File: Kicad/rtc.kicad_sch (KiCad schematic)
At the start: 6 parts, among them U1101 MCP7940N, Y1101 32,768 Hz

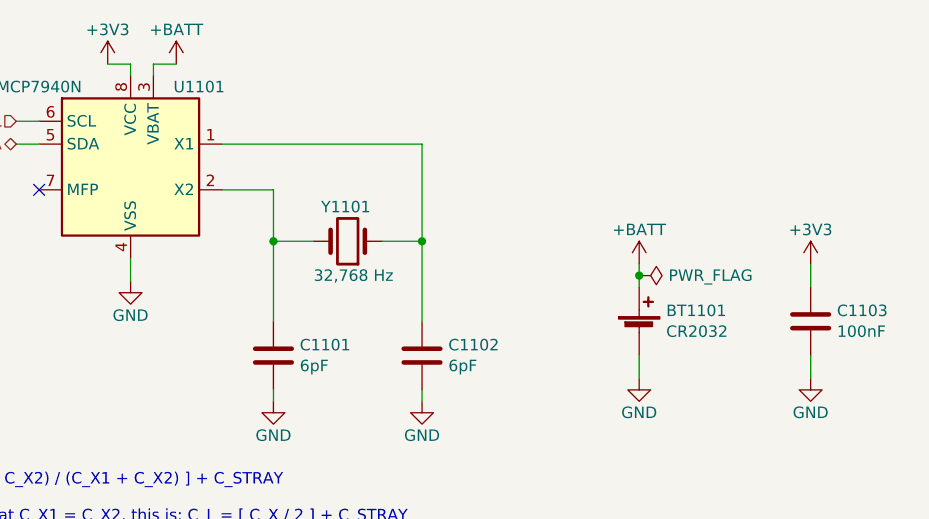
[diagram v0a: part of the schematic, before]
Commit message: Update schematic files to Kicad 6.
Had to fix some symbols which didn't have perfect matches in K6.
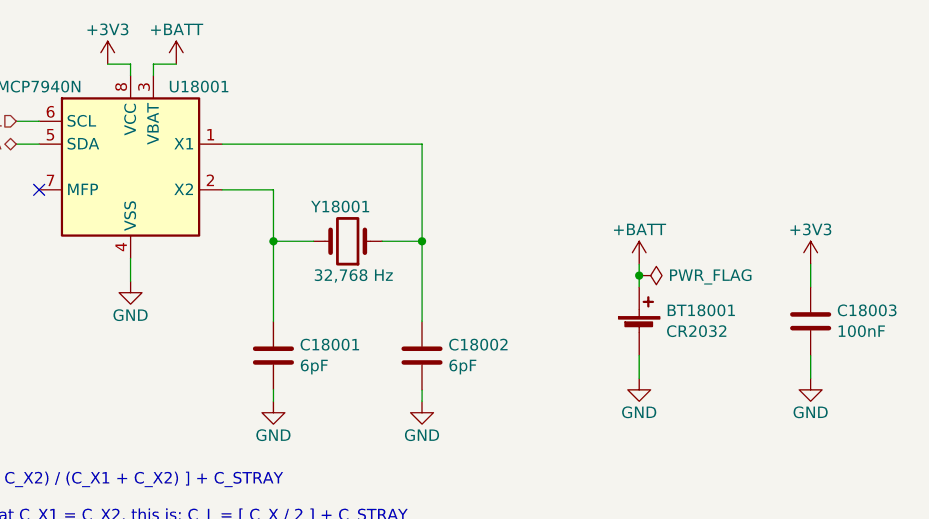
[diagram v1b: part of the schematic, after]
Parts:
- U18001: renamed from U1101; symbol Neotron-Common-Hardware-rescue:MCP7940N-xP-Timer -> Timer_RTC:MCP7940N-xP
- renumbered BT1101 to BT18001, C1101 to C18001, C1102 to C18002, C1103 to C18003, Y1101 to Y18001
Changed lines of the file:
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@@
   (symbol (lib_id "power:+3V3") (at 179.07 78.74 0) (unit 1)
     (in_bom yes) (on_board yes)
-    (property "Reference" "#PWR01108" (id 0) (at 179.07 82.55 0)
+    (property "Reference" "#PWR018008" (id 0) (at 179.07 82.55 0)
       (effects (font (size 1.27 1.27)) hide)
     )
@@
   (symbol (lib_id "Device:C") (at 179.07 85.09 0) (unit 1)
     (in_bom yes) (on_board yes)
-    (property "Reference" "C1103" (id 0) (at 181.991 83.9216 0)
+    (property "Reference" "C18003" (id 0) (at 181.991 83.9216 0)
       (effects (font (size 1.27 1.27)) (justify left))
     )
@@
   (symbol (lib_id "power:GND") (at 179.07 91.44 0) (unit 1)
     (in_bom yes) (on_board yes)
-    (property "Reference" "#PWR01109" (id 0) (at 179.07 97.79 0)
+    (property "Reference" "#PWR018009" (id 0) (at 179.07 97.79 0)
       (effects (font (size 1.27 1.27)) hide)
     )
@@
   (symbol (lib_id "power:+3V3") (at 100.965 56.515 0) (unit 1)
     (in_bom yes) (on_board yes)
-    (property "Reference" "#PWR01101" (id 0) (at 100.965 60.325 0)
+    (property "Reference" "#PWR018001" (id 0) (at 100.965 60.325 0)
       (effects (font (size 1.27 1.27)) hide)
     )
@@
   (symbol (lib_id "power:GND") (at 103.505 80.645 0) (unit 1)
     (in_bom yes) (on_board yes)
-    (property "Reference" "#PWR01102" (id 0) (at 103.505 86.995 0)
+    (property "Reference" "#PWR018002" (id 0) (at 103.505 86.995 0)
       (effects (font (size 1.27 1.27)) hide)
     )
@@
   (symbol (lib_id "Device:Crystal") (at 127.635 76.2 180) (unit 1)
     (in_bom yes) (on_board yes)
-    (property "Reference" "Y1101" (id 0) (at 130.175 72.39 0)
+    (property "Reference" "Y18001" (id 0) (at 130.175 72.39 0)
       (effects (font (size 1.27 1.27)) (justify left))
     )
@@
   (symbol (lib_id "power:+BATT") (at 108.585 56.515 0) (unit 1)
     (in_bom yes) (on_board yes)
-    (property "Reference" "#PWR01103" (id 0) (at 108.585 60.325 0)
+    (property "Reference" "#PWR018003" (id 0) (at 108.585 60.325 0)
       (effects (font (size 1.27 1.27)) hide)
     )
@@
   (symbol (lib_id "power:+BATT") (at 160.02 78.74 0) (unit 1)
     (in_bom yes) (on_board yes)
-    (property "Reference" "#PWR01106" (id 0) (at 160.02 82.55 0)
+    (property "Reference" "#PWR018006" (id 0) (at 160.02 82.55 0)
       (effects (font (size 1.27 1.27)) hide)
     )
@@
   (symbol (lib_id "power:GND") (at 160.02 91.44 0) (unit 1)
     (in_bom yes) (on_board yes)
-    (property "Reference" "#PWR01107" (id 0) (at 160.02 97.79 0)
+    (property "Reference" "#PWR018007" (id 0) (at 160.02 97.79 0)
       (effects (font (size 1.27 1.27)) hide)
     )
@@
   (symbol (lib_id "Device:C") (at 135.89 88.9 0) (unit 1)
     (in_bom yes) (on_board yes)
-    (property "Reference" "C1102" (id 0) (at 138.811 87.7316 0)
+    (property "Reference" "C18002" (id 0) (at 138.811 87.7316 0)
       (effects (font (size 1.27 1.27)) (justify left))
     )
@@
   (symbol (lib_id "Device:C") (at 119.38 88.9 0) (unit 1)
     (in_bom yes) (on_board yes)
-    (property "Reference" "C1101" (id 0) (at 122.301 87.7316 0)
+    (property "Reference" "C18001" (id 0) (at 122.301 87.7316 0)
       (effects (font (size 1.27 1.27)) (justify left))
     )
@@
   (symbol (lib_id "power:GND") (at 119.38 93.98 0) (unit 1)
     (in_bom yes) (on_board yes)
-    (property "Reference" "#PWR01104" (id 0) (at 119.38 100.33 0)
+    (property "Reference" "#PWR018004" (id 0) (at 119.38 100.33 0)
       (effects (font (size 1.27 1.27)) hide)
     )
@@
     (pin "1")
   )
-  (symbol (lib_id "Neotron-Common-Hardware-rescue:MCP7940N-xP-Timer") (at 103.505 67.945 0) (unit 1)
-    (in_bom yes) (on_board yes)
-    (property "Reference" "U1101" (id 0) (at 111.125 59.055 0))
+  (symbol (lib_id "Timer_RTC:MCP7940N-xP") (at 103.505 67.945 0) (unit 1)
+    (in_bom yes) (on_board yes)
+    (property "Reference" "U18001" (id 0) (at 111.125 59.055 0))
     (property "Value" "MCP7940N" (id 1) (at 93.345 59.055 0))
     (property "Footprint" "Package_DIP:DIP-8_W7.62mm" (id 2) (at 103.505 67.945 0)
@@
   (symbol (lib_id "Device:Battery_Cell") (at 160.02 86.36 0) (unit 1)
     (in_bom yes) (on_board yes)
-    (property "Reference" "BT1101" (id 0) (at 163.0172 83.9216 0)
+    (property "Reference" "BT18001" (id 0) (at 163.0172 83.9216 0)
       (effects (font (size 1.27 1.27)) (justify left))
     )
@@
   (symbol (lib_id "power:PWR_FLAG") (at 160.02 80.01 270) (unit 1)
     (in_bom yes) (on_board yes)
-    (property "Reference" "#FLG01101" (id 0) (at 161.925 80.01 0)
+    (property "Reference" "#FLG018001" (id 0) (at 161.925 80.01 0)
       (effects (font (size 1.27 1.27)) hide)
     )
@@
   (symbol (lib_id "power:GND") (at 135.89 93.98 0) (unit 1)
     (in_bom yes) (on_board yes)
-    (property "Reference" "#PWR01105" (id 0) (at 135.89 100.33 0)
-      (effects (font (size 1.27 1.27)) hide)
-    )
+    (property "Reference" "#PWR018005" (id 0) (at 135.89 100.33 0)
+      (effects (font (size 1.27 1.27)) hide)
+    )

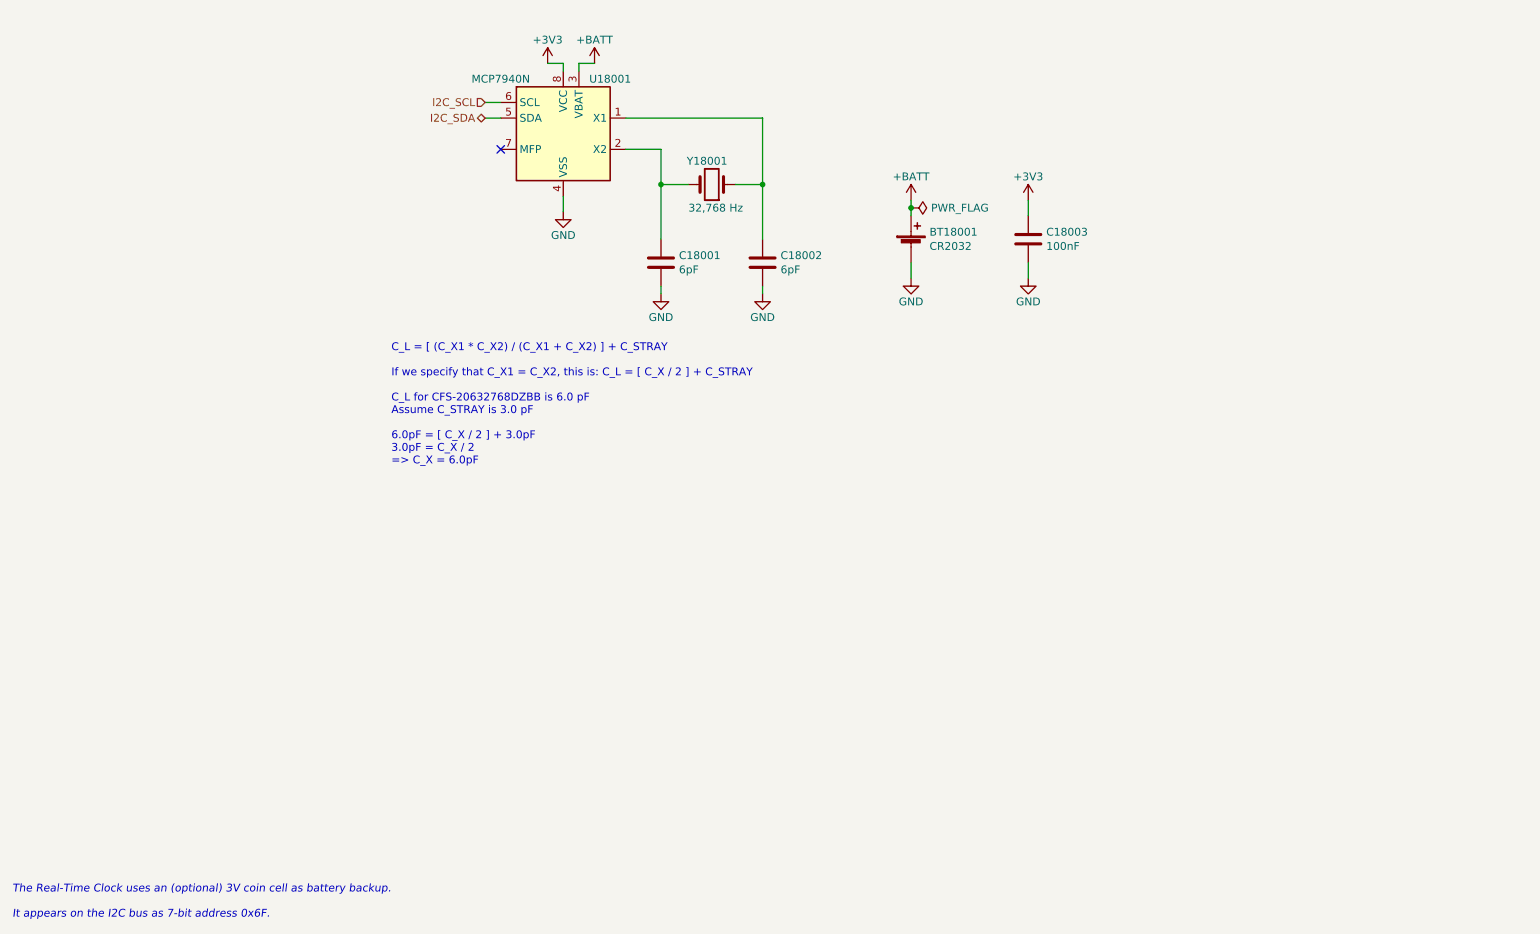
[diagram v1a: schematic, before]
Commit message: Imported sheets from Neotron Pico.
Standardised on +3V3 not +3.3V
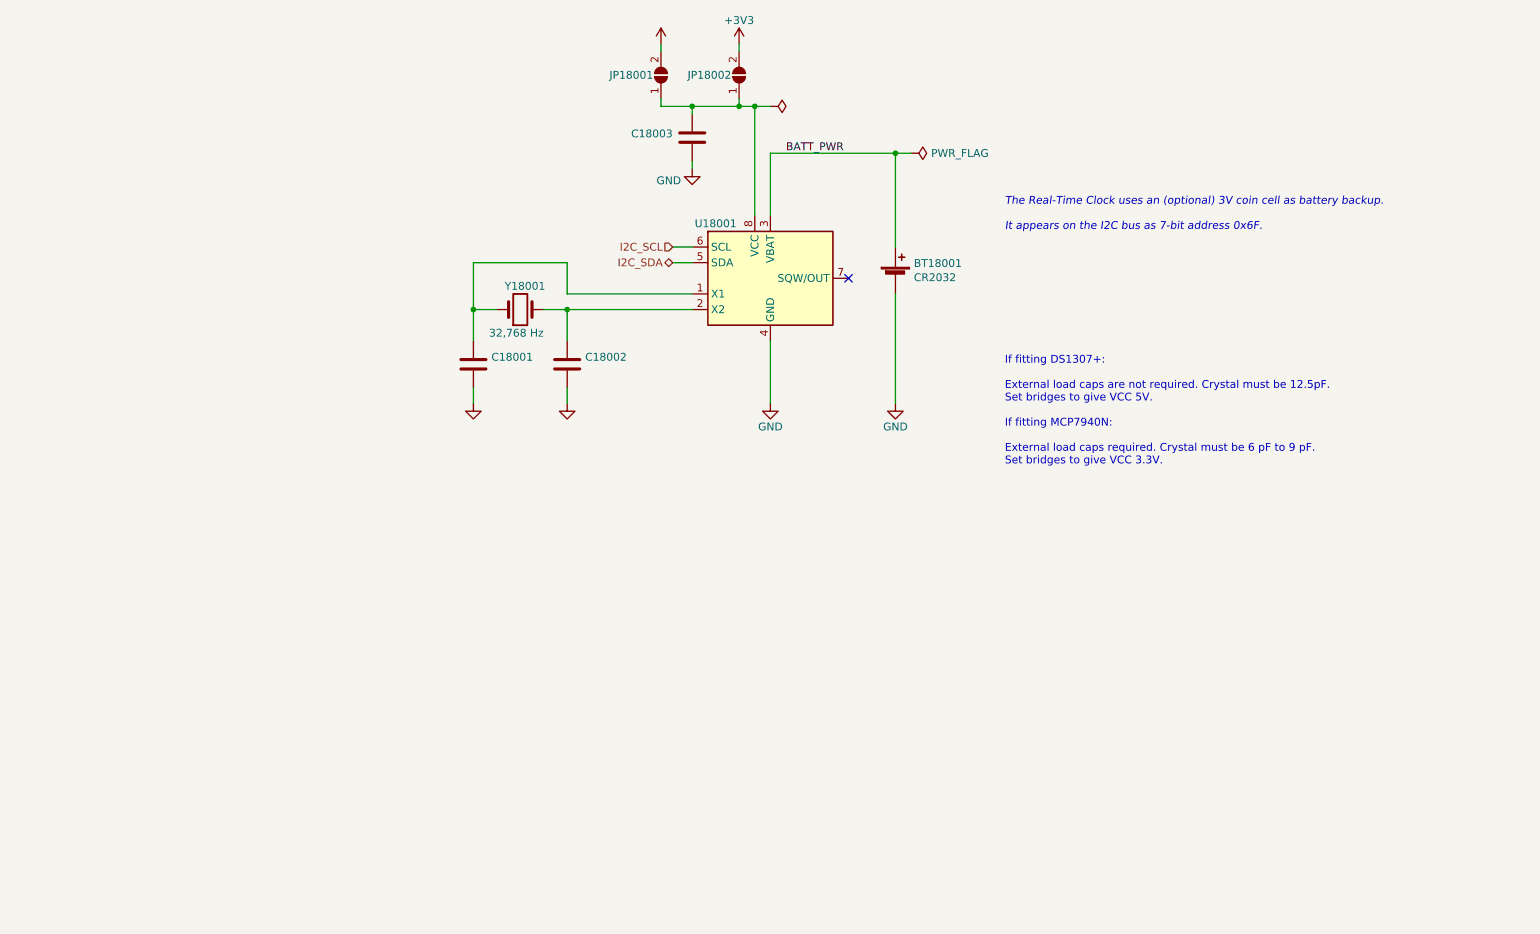
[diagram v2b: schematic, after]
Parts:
- removed U18001: MCP7940N, Package_DIP:DIP-8_W7.62mm, symbol Timer_RTC:MCP7940N-xP
- added JP18001, JP18002: (no value), symbol Jumper:SolderJumper_2_Open
- added U18001: (no value), symbol Timer_RTC:DS1307Z+
- BT18001: Digikey 36-103-ND -> 2057-BH-80A-1-ND; MPN 103 -> BH-80A-1; Manufacturer Keystone -> Adam Tech
- C18001, C18002: value 6pF -> (none); footprint Capacitor_SMD:C_0805_2012Metric_Pad1.18x1.45mm_HandSolder -> (none); DNP 0 -> 1; Digikey 311-1095-1-ND -> (none); LCSC Part# C67560 -> (none); MPN CC0805DRNPO9BN6R0 -> (none); Manufacturer Yageo -> (none); Mouser 603-CC805DRNPO9BN6R0 -> (none); Tolerance C0G -> (none); Voltage 10V -> (none)
- C18003: value 100nF -> (none); footprint Capacitor_SMD:C_0805_2012Metric_Pad1.18x1.45mm_HandSolder -> (none); JLCPCB Collection (none) -> Basic; LCSC Part# C49678 -> C15850; MPN CPL-CAP-X7R-0805-100NF-50V -> CL21A106KAYNNNE; Manufacturer CPL -> Samsung; Voltage 10V -> 25V
- Y18001: Digikey 300-8301-ND -> (none); JLCPCB Collection (none) -> Basic; LCSC Part# (none) -> C32346; MPN CFS-20632768DZBB -> Q13FC1350000400; Manufacturer Citizen -> Seiko Epson; Mouser CFS-20632768DZBB -> (none)
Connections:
- net +3V3: now also JP18002.2 (B); no longer C18003.1
- net GND: now also C18003.1, U18001.4 (GND); no longer C18003.2
- net I2C_SCL: now also U18001.6 (SCL)
- net I2C_SDA: now also U18001.5 (SDA)
- net at Y18001.1: now also C18001.1, U18001.1 (X1); no longer C18002.1
- net at Y18001.2: now also C18002.1, U18001.2 (X2); no longer C18001.1
- net +BATT renamed BATT_PWR
- net BATT_PWR: now also U18001.3 (VBAT)
- new net: C18003.2, JP18001.1 (A), JP18002.1 (A), U18001.8 (VCC)
- new net +5V: JP18001.2 (B)
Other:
- note added: "If fitting DS1307+: External load caps are not required. Crystal must be 12.5pF. Set bridges to give VCC 5V. If fitting MCP7940N: External load caps required. Crystal must be 6 pF to 9 pF. Set bridges to give VCC 3.3V."
- note removed: "C_L = [ (C_X1 * C_X2) / (C_X1 + C_X2) ] + C_STRAY If we specify that C_X1 = C_X2, this is: C_L = [ C_X / 2 ] + C_STRAY C_L for CFS-20632768DZBB is 6.0 pF Assume C_STRAY is 3.0 pF 6.0pF = [ C_X / 2 ] + 3.0pF 3.0pF = C_X / 2 => C_X = 6.0pF"
- company: https://neotron-compute.github.io/ -> https://neotron-compute.github.io
- moved on the sheet: BT18001, Y18001
